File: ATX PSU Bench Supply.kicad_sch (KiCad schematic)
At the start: 35 parts, among them J1 4mm Banana Socket R, J10 Molex 46991-1008, J11 OLED-128x64, J12 Conn_01x02, J18 Conn_01x08, J19 Conn_01x05, J2 4mm Banana Socket R, J20 Conn_01x07, J3 4mm Banana Socket B, J4 4mm Banana Socket R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

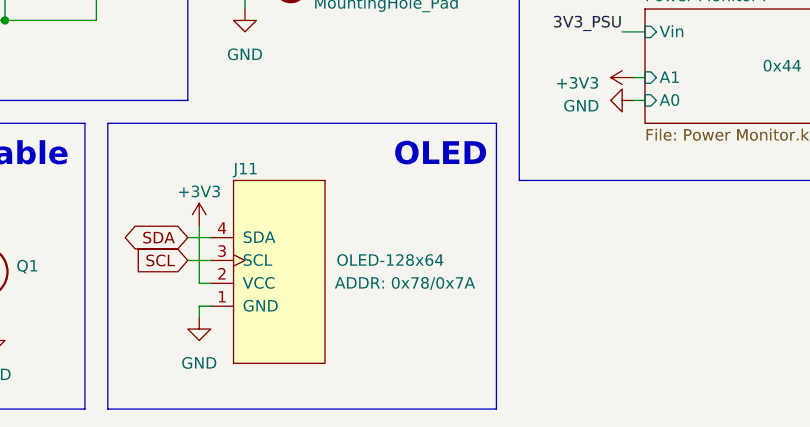
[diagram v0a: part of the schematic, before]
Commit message: Fix schematic I2C address, add firmware dir
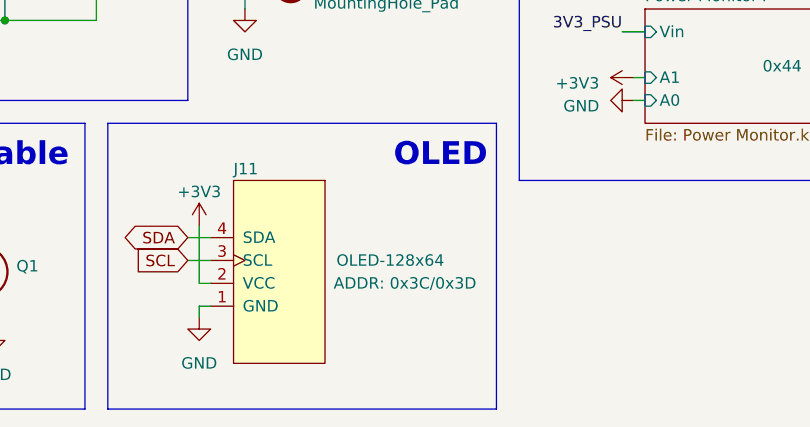
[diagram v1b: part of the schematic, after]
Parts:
- J11: ADDR 0x78/0x7A -> 0x3C/0x3D
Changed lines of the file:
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@@
       (effects (font (size 1.27 1.27)) hide)
     )
-    (property "ADDR" "0x78/0x7A" (at 158.75 137.16 90) (show_name)
+    (property "ADDR" "0x3C/0x3D" (at 158.75 137.16 90) (show_name)
       (effects (font (size 1.27 1.27)))
     )

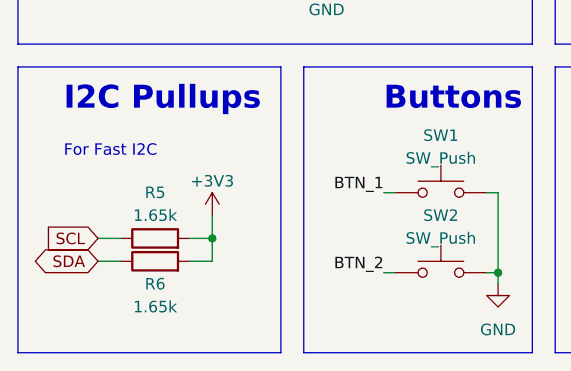
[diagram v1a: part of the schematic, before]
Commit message: Add DNP to I2C Pullups
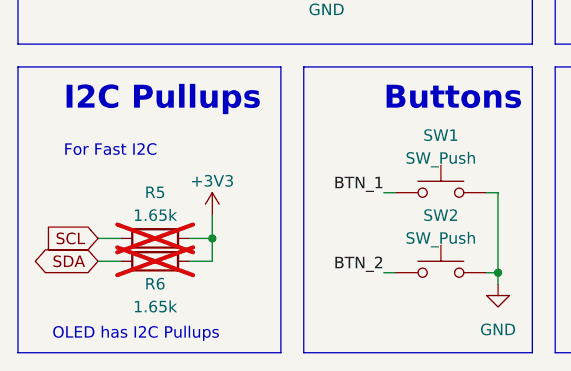
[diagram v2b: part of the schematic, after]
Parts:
- R5, R6: now not fitted
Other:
- note added: "OLED has I2C Pullups"
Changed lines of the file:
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@@
     (effects (font (size 2.54 2.54) (thickness 0.508) bold) (justify left bottom))
+  )
+  (text "OLED has I2C Pullups" (at 30.48 149.86 0)
+    (effects (font (size 1.27 1.27)) (justify left bottom))
   )
   (text "For Fast I2C" (at 31.75 129.54 0)
@@
   )
   (symbol (lib_id "Device:R") (at 41.91 140.97 90) (unit 1)
-    (in_bom yes) (on_board yes) (dnp no)
+    (in_bom yes) (on_board yes) (dnp yes)
     (property "Reference" "R6" (at 41.91 143.51 90)
       (effects (font (size 1.27 1.27)))
@@
   )
   (symbol (lib_id "Device:R") (at 41.91 138.43 90) (unit 1)
-    (in_bom yes) (on_board yes) (dnp no) (fields_autoplaced)
+    (in_bom yes) (on_board yes) (dnp yes) (fields_autoplaced)
     (property "Reference" "R5" (at 41.91 133.35 90)
       (effects (font (size 1.27 1.27)))

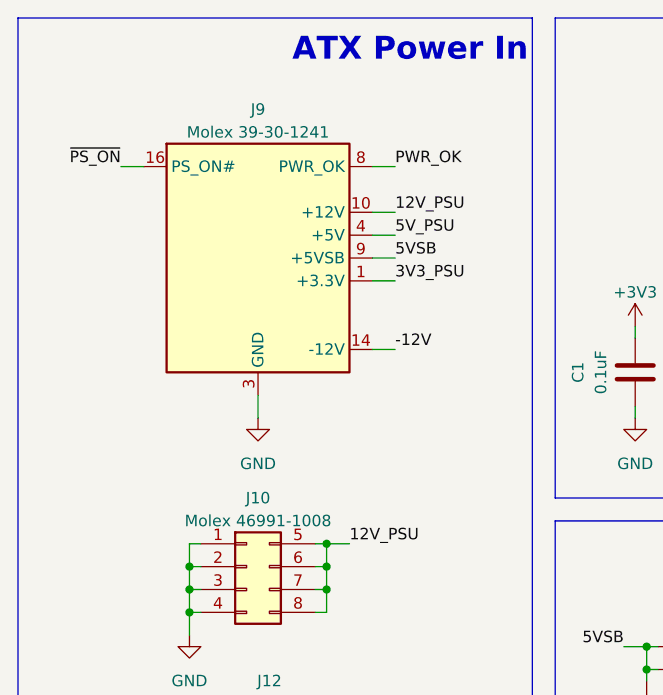
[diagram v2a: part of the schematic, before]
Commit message: Fix some component model numbers
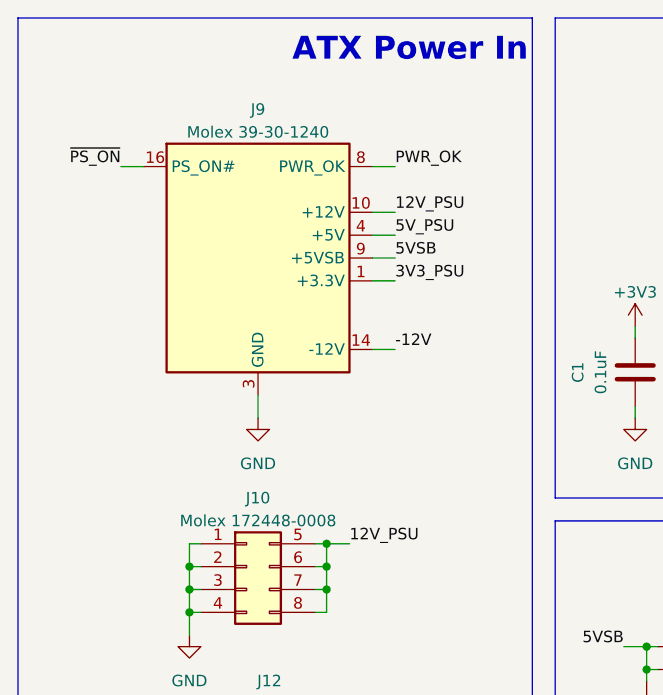
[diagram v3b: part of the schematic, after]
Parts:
- J10: value Molex 46991-1008 -> Molex 172448-0008; Mfr. No 46991-1008 -> 172448-0008; Mouser No 538-46991-1008 -> 538-172448-0008
- J9: value Molex 39-30-1241 -> Molex 39-30-1240; Mfr. No 39-30-1241 -> 39-30-1240; Mouser No 538-39-30-1241 -> 538-39-30-1240
- R5: Mfr. No CRCW0805220KFKEA -> CRCW0805220RFKEAC; Mouser No 71-CRCW0805220KFKEA -> 71-CRCW0805220RFKEAC
- SW1, SW2: Mfr. No (none) -> SKHHBWA010; Mouser No (none) -> 688-SKHHBW
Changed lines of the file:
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@@
       (effects (font (size 1.27 1.27)))
     )
-    (property "Value" "Molex 46991-1008" (at 53.34 81.28 0)
+    (property "Value" "Molex 172448-0008" (at 53.34 81.28 0)
       (effects (font (size 1.27 1.27)))
     )
@@
       (effects (font (size 1.27 1.27)) hide)
     )
-    (property "Mfr. No" "46991-1008" (at 52.07 86.36 0)
-      (effects (font (size 1.27 1.27)) hide)
-    )
-    (property "Mouser No" "538-46991-1008" (at 52.07 86.36 0)
+    (property "Mfr. No" "172448-0008" (at 52.07 86.36 0)
+      (effects (font (size 1.27 1.27)) hide)
+    )
+    (property "Mouser No" "538-172448-0008" (at 52.07 86.36 0)
       (effects (font (size 1.27 1.27)) hide)
     )
@@
       (effects (font (size 1.27 1.27)) hide)
     )
+    (property "Mfr. No" "SKHHBWA010" (at 73.66 133.35 0)
+      (effects (font (size 1.27 1.27)) hide)
+    )
+    (property "Mouser No" "688-SKHHBW" (at 73.66 133.35 0)
+      (effects (font (size 1.27 1.27)) hide)
+    )
     (pin "1")
     (pin "2")
@@
     )
     (property "Datasheet" "~" (at 73.66 137.16 0)
+      (effects (font (size 1.27 1.27)) hide)
+    )
+    (property "Mfr. No" "SKHHBWA010" (at 73.66 142.24 0)
+      (effects (font (size 1.27 1.27)) hide)
+    )
+    (property "Mouser No" "688-SKHHBW" (at 73.66 142.24 0)
       (effects (font (size 1.27 1.27)) hide)
     )
@@
       (effects (font (size 1.27 1.27)))
     )
-    (property "Value" "Molex 39-30-1241" (at 53.34 38.1 0)
+    (property "Value" "Molex 39-30-1240" (at 53.34 38.1 0)
       (effects (font (size 1.27 1.27)))
     )
@@
       (effects (font (size 1.27 1.27)) hide)
     )
-    (property "Mfr. No" "39-30-1241" (at 53.34 52.07 0)
-      (effects (font (size 1.27 1.27)) hide)
-    )
-    (property "Mouser No" "538-39-30-1241" (at 53.34 52.07 0)
+    (property "Mfr. No" "39-30-1240" (at 53.34 52.07 0)
+      (effects (font (size 1.27 1.27)) hide)
+    )
+    (property "Mouser No" "538-39-30-1240" (at 53.34 52.07 0)
       (effects (font (size 1.27 1.27)) hide)
     )
@@
       (effects (font (size 1.27 1.27)) hide)
     )
-    (property "Mfr. No" "CRCW0805220KFKEA" (at 107.95 127 90)
-      (effects (font (size 1.27 1.27)) hide)
-    )
-    (property "Mouser No" "71-CRCW0805220KFKEA" (at 107.95 127 0)
-      (effects (font (size 1.27 1.27)) hide)
-    )
+    (property "Mfr. No" "CRCW0805220RFKEAC" (at 107.95 127 90)
+      (effects (font (size 1.27 1.27)) hide)
+    )
+    (property "Mouser No" "71-CRCW0805220RFKEAC" (at 107.95 127 0)
+      (effects (font (size 1.27 1.27)) hide)
+    )

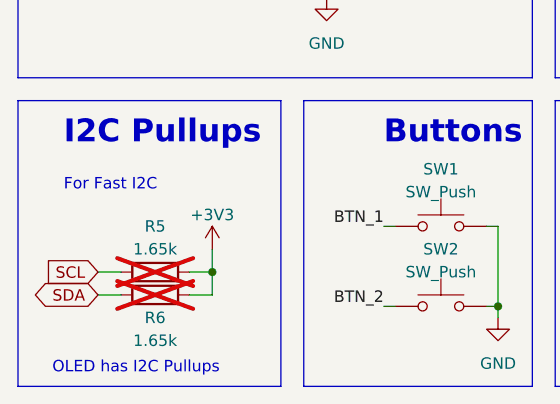
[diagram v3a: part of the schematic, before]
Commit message: Set PCB metadata
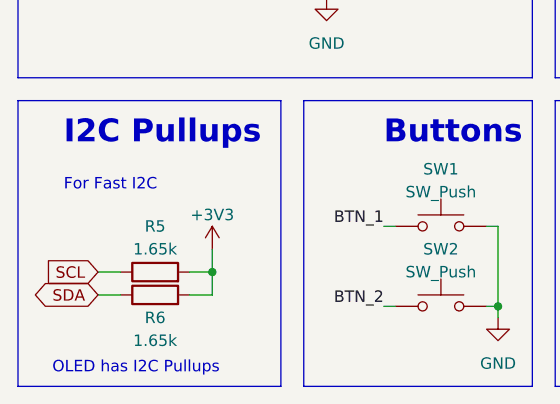
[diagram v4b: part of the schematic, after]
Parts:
- R5, R6: now fitted
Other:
- title: (none) -> BenchATX
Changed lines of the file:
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@@
 (kicad_sch (version 20230121) (generator eeschema)
   (paper "A4")
+  (title_block
+    (title "BenchATX")
+    (date "2026-05-01")
+    (rev "A")
+  )
   (junction (at 60.96 83.82) (diameter 0) (color 0 0 0 0)
   )
@@
   )
   (symbol (lib_id "Device:R") (at 41.91 140.97 90) (unit 1)
-    (in_bom yes) (on_board yes) (dnp yes)
+    (in_bom yes) (on_board yes) (dnp no)
     (property "Reference" "R6" (at 41.91 143.51 90)
       (effects (font (size 1.27 1.27)))
@@
   )
   (symbol (lib_id "Device:R") (at 41.91 138.43 90) (unit 1)
-    (in_bom yes) (on_board yes) (dnp yes) (fields_autoplaced)
+    (in_bom yes) (on_board yes) (dnp no) (fields_autoplaced)
     (property "Reference" "R5" (at 41.91 133.35 90)
       (effects (font (size 1.27 1.27)))
